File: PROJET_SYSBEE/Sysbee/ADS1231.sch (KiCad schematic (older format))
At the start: 6 parts, among them U4 ADS1231

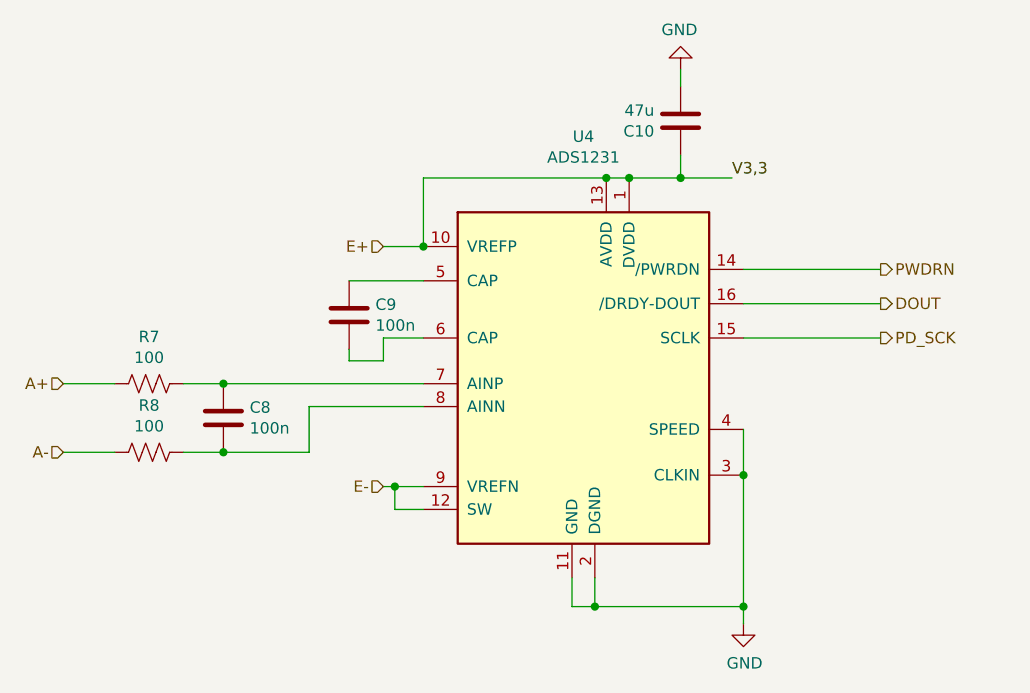
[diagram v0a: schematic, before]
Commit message: placement et routage, reste à redessiner un peu les pistes et rajouter les écritures F.Silks
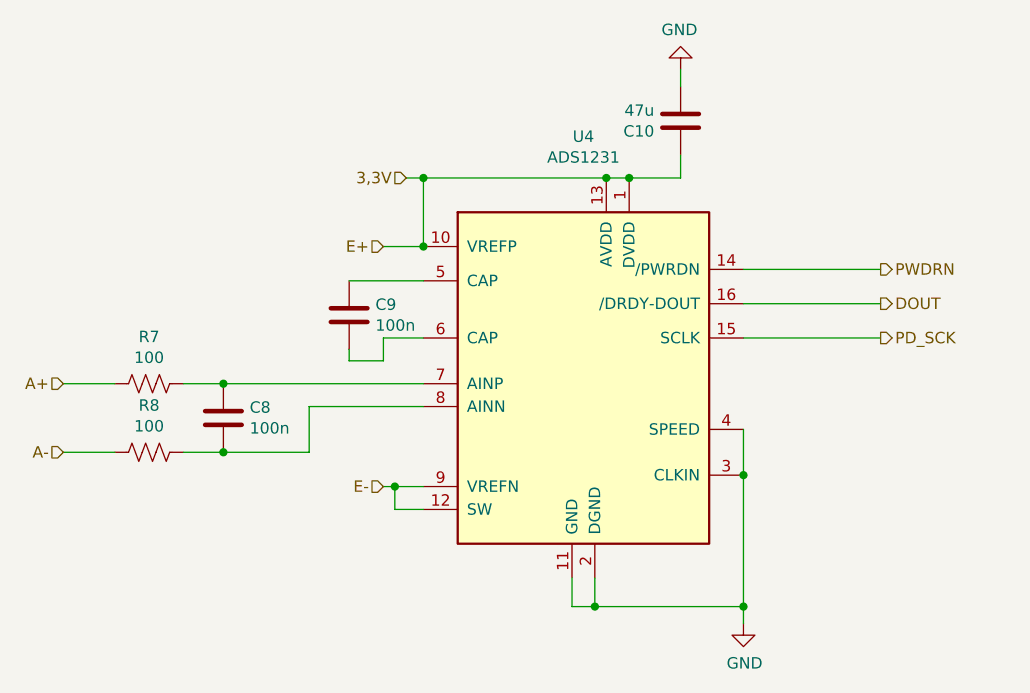
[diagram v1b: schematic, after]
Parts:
- C10: footprint Capacitor_SMD:CP_Elec_6.3x5.4 -> Capacitor_Tantalum_SMD:CP_EIA-3216-18_Kemet-A
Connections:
- net E+ renamed 3,3V
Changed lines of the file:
@@
 F 0 "C10" H 6315 2546 50  0000 L CNN
 F 1 "47u" H 6315 2455 50  0000 L CNN
-F 2 "Capacitor_SMD:CP_Elec_6.3x5.4" H 6238 2350 50  0001 C CNN
+F 2 "Capacitor_Tantalum_SMD:CP_EIA-3216-18_Kemet-A" H 6238 2350 50  0001 C CNN
 F 3 "~" H 6200 2500 50  0001 C CNN
 	1    6200 2500
@@
 	-1   0    0    1
 $EndComp
-Text Label 6425 2750 0    50   ~ 0
-V3,3
 $Comp
 L Sysbee-rescue:C-Device C9
@@
 	5975 2750 6200 2750
 Connection ~ 5975 2750
-Connection ~ 6200 2750
+Text HLabel 5000 2750 0    50   Input ~ 0
+3,3V
 Wire Wire Line
-	6200 2750 6425 2750
+	5000 2750 5075 2750
+Connection ~ 5075 2750
 $EndSCHEMATC

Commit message: placement et routage ok
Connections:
- net DOUT renamed ADC_DOUT
- net PD_SCK renamed ADC_CLK
- net PWDRN renamed ADC_PWDRN
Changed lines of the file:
@@
 Wire Wire Line
 	3725 3950 3500 3950
-Text HLabel 7075 3150 2    50   Output ~ 0
-PWDRN
+Text HLabel 7075 3150 2    50   Input ~ 0
+ADC_PWDRN
 Text HLabel 7075 3300 2    50   Output ~ 0
-DOUT
-Text HLabel 7075 3450 2    50   Output ~ 0
-PD_SCK
+ADC_DOUT
+Text HLabel 7075 3450 2    50   Input ~ 0
+ADC_CLK
 Text HLabel 4900 3050 0    50   Input ~ 0
 E+
